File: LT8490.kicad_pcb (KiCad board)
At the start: 6 copper layers, 37.2 x 46 mm, 148 parts, among them J1 Conn_01x01, J10 Conn_01x01, J11 Conn_01x01, J12 Conn_01x01, J13 Conn_01x01, J14 Conn_01x01, J15 Conn_01x01, J16 Conn_01x01, J17 Conn_01x01, J18 Conn_01x01, J19 Conn_01x01, J2 Conn_01x01, J20 Conn_01x01, J21 Conn_01x01, J22 Conn_01x01, J23 Conn_01x01, J24 Conn_01x01, J25 Conn_01x01, J3 Conn_01x01, J4 Conn_01x01, J5 Conn_01x01, J6 Conn_01x01, J7 Conn_01x01, J8 Conn_01x01, J9 Conn_01x01, Q1 Si7106DN, Q2 Si7106DN, Q3 Si7106DN, Q4 Si7106DN, Q5 BSS84, Q6 MBT2222ADW1T1, U4 LT8490EUKJPBF

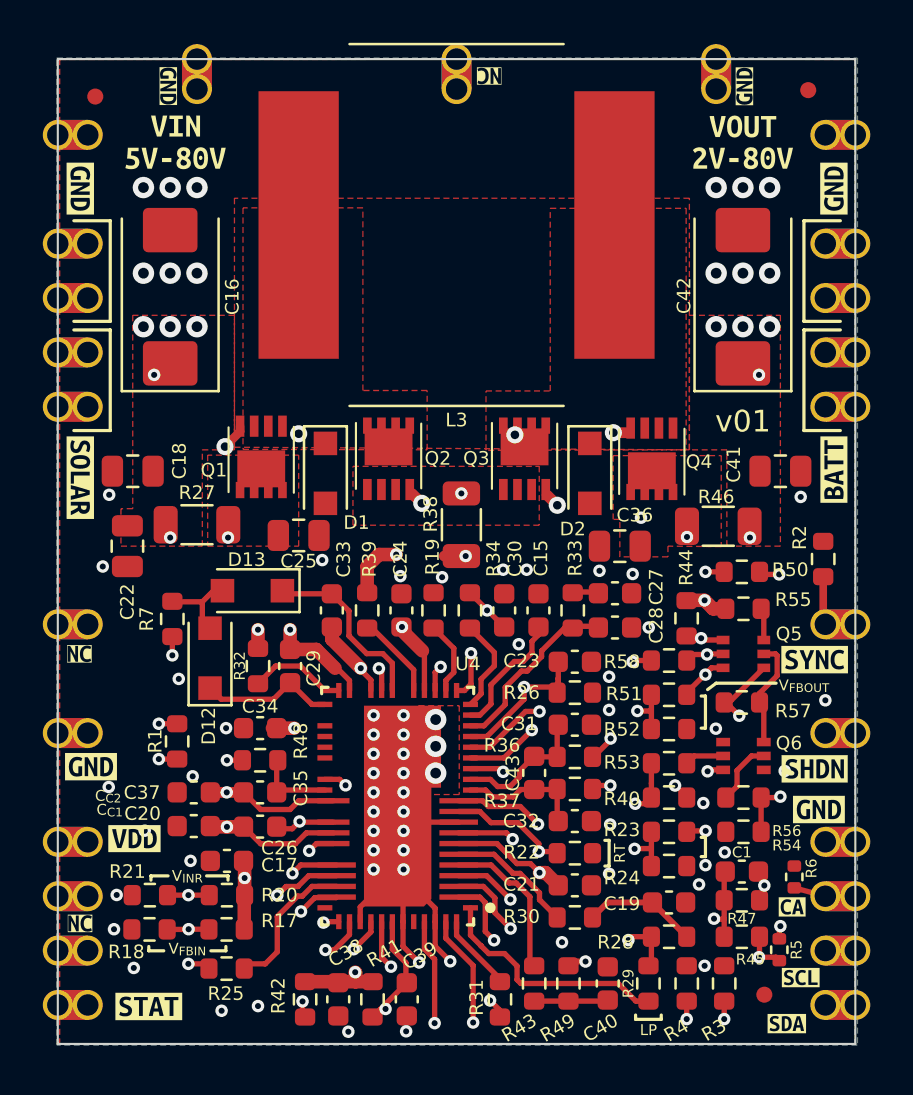
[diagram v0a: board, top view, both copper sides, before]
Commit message: beefed up LDO3V3
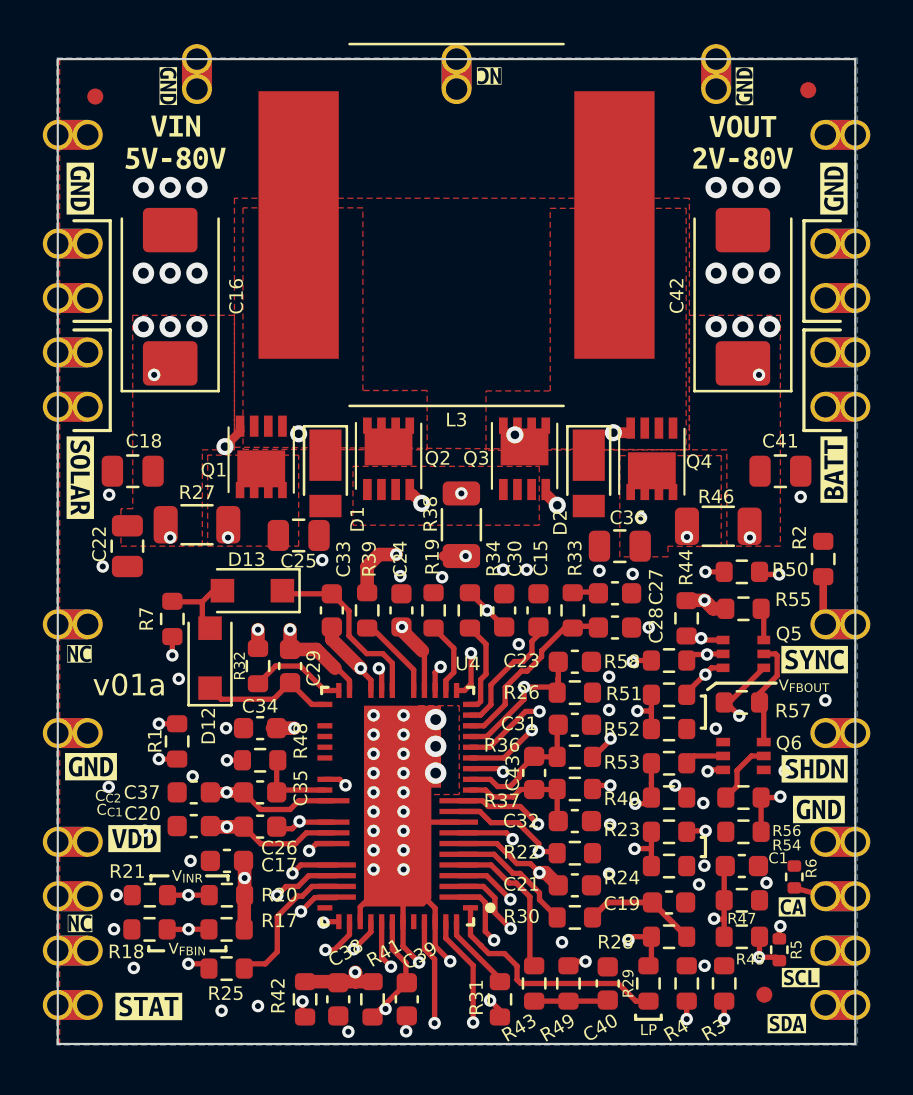
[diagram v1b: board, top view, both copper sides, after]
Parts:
- D1, D2: footprint Diode_SMD:D_SOD-123F -> Diode_SMD:D_PowerDI-123
- moved C1 0.26 mm to (161.2, 113.4)
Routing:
- net Net-(C30-Pad1): track 23.9 -> 23.2 mm
- net GND: vias 72 -> 71
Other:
- board text added: "v01a"
- board text removed: "RT"
- board text removed: "v01"
